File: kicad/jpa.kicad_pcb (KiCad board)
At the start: 2 copper layers, 3 parts, among them J1 ARM_NOAH_6PIN, J2 ARM_10PIN, J3 ARM_NOAH_5PIN

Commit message: layout, gerbers, models done
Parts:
- added J4: PICKIT_HDR, kicadlib:TH_6X1_HDR, F.Cu at (140.0, 98.7)
- moved J3 0.95 mm to (156.3, 108.0)
- moved J1 0.66 mm to (156.3, 97.7)
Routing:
- net /icspclk/swdclk: track 0.00 -> 36.8 mm, vias 0 -> 2
- net /icspdat/swdio: track 0.00 -> 31.2 mm, vias 0 -> 1
- net /swo/lvp: track 0.00 -> 29.2 mm, vias 0 -> 2
- net /mclr/nreset: track 0.00 -> 20.0 mm, vias 0 -> 1
- net /vcc: track 0.00 -> 19.4 mm
- added copper zone on B.Cu, net GND
- added copper zone on F.Cu, net GND
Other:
- board outline added: 24.9 x 20.8 mm
- board text added: "1"
- board text added: "JST PROG ADAPT V1"
- board text added: "github.com/noahp/jpa v1"
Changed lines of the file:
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@@
-(kicad_pcb (version 4) (host pcbnew 4.0.0-rc2-stable)
+(kicad_pcb (version 4) (host pcbnew 4.0.0-rc1-stable)
   (general
-    (links 13)
-    (no_connects 13)
-    (area 0 0 0 0)
+    (links 19)
+    (no_connects 6)
+    (area 136.322999 94.158999 161.522 115.137001)
     (thickness 1.6)
-    (drawings 0)
-    (tracks 0)
+    (drawings 11)
+    (tracks 52)
     (zones 0)
-    (modules 3)
+    (modules 4)
     (nets 9)
   )
@@
   (setup
     (last_trace_width 0.25)
+    (user_trace_width 0.35)
     (trace_clearance 0.2)
     (zone_clearance 0.508)
@@
     (pad_to_mask_clearance 0.2)
     (aux_axis_origin 0 0)
-    (visible_elements FFFFFF7F)
+    (visible_elements 7FFFFFFF)
     (pcbplotparams
-      (layerselection 0x00030_80000001)
+      (layerselection 0x010f0_80000001)
       (usegerberextensions false)
       (excludeedgelayer true)
@@
       (outputformat 1)
       (mirror false)
-      (drillshape 1)
+      (drillshape 0)
       (scaleselection 1)
-      (outputdirectory ""))
+      (outputdirectory gerbers))
   )
   (net 0 "")
@@
   )
   (module kicadlib:SMD_JST_6_PIN_VERT (layer F.Cu)
-    (at 156.3 97 270)
-    (fp_text reference J1 (at 2.6 1.8 270) (layer F.SilkS)
+    (at 156.337 97.663 270)
+    (fp_text reference J1 (at 0.028 1.868 360) (layer F.SilkS)
       (effects (font (size 0.75 0.75) (thickness 0.12)))
     )
@@
   )
   (module kicadlib:ARM_10_PIN (layer F.Cu)
-    (at 148.5011 105.0036)
+    (at 148.463 105.029)
     (fp_text reference J2 (at -0.635 -7.4) (layer F.SilkS)
       (effects (font (size 0.75 0.75) (thickness 0.12)))
@@
   )
   (module kicadlib:SMD_JST_5_PIN_VERT (layer F.Cu)
-    (at 156.3 107 270)
-    (fp_text reference J3 (at 2.6 1.8 270) (layer F.SilkS)
+    (at 156.337 107.95 270)
+    (fp_text reference J3 (at -0.066 1.995 360) (layer F.SilkS)
       (effects (font (size 0.75 0.75) (thickness 0.12)))
     )
@@
     )
   )
+  (module kicadlib:TH_6X1_HDR (layer F.Cu)
+    (at 139.954 98.679 270)
+    (fp_text reference J4 (at -1.905 0.127 360) (layer F.SilkS)
+      (effects (font (size 0.75 0.75) (thickness 0.12)))
+    )
+    (fp_text value PICKIT_HDR (at 14.986 0 360) (layer F.Fab)
+      (effects (font (size 0.75 0.75) (thickness 0.12)))
+    )
+    (pad 1 thru_hole rect (at 0 0 270) (size 2 2) (drill 1.2) (layers *.Cu *.Mask F.SilkS)
+      (net 4 /mclr/nreset))
+    (pad 2 thru_hole circle (at 2.54 0 270) (size 2 2) (drill 1.2) (layers *.Cu *.Mask F.SilkS)
+      (net 1 /vcc))
+    (pad 3 thru_hole circle (at 5.08 0 270) (size 2 2) (drill 1.2) (layers *.Cu *.Mask F.SilkS)
+      (net 6 GND))
+    (pad 4 thru_hole circle (at 7.62 0 270) (size 2 2) (drill 1.2) (layers *.Cu *.Mask F.SilkS)
+      (net 2 /icspdat/swdio))
+    (pad 5 thru_hole circle (at 10.16 0 270) (size 2 2) (drill 1.2) (layers *.Cu *.Mask F.SilkS)
+      (net 3 /icspclk/swdclk))
+    (pad 6 thru_hole circle (at 12.7 0 270) (size 2 2) (drill 1.2) (layers *.Cu *.Mask F.SilkS)
+      (net 5 /swo/lvp))
+    (model ${KIPRJMOD}/kicadlib/kicadlib.pretty/models/TH_6_PIN_HDR.wrl
+      (at (xyz -0.1 0 0.1))
+      (scale (xyz 0.395 0.395 0.395))
+      (rotate (xyz -90 0 0))
+    )
+  )
+  (gr_text "JST PROG ADAPT V1" (at 148.082 113.538) (layer F.Mask)
+    (effects (font (size 1 1) (thickness 0.15)))
+  )
+  (gr_text 1 (at 142.24 98.552) (layer F.SilkS)
+    (effects (font (size 1.5 1.5) (thickness 0.3)))
+  )
+  (gr_text "github.com/noahp/jpa\nv1" (at 157.734 104.648 270) (layer B.Mask)
+    (effects (font (size 1 1) (thickness 0.15)) (justify mirror))
+  )
+  (gr_line (start 136.398 113.03) (end 136.398 96.266) (angle 90) (layer Edge.Cuts) (width 0.15))
+  (gr_line (start 159.258 115.062) (end 138.43 115.062) (angle 90) (layer Edge.Cuts) (width 0.15))
+  (gr_line (start 161.29 96.266) (end 161.29 113.03) (angle 90) (layer Edge.Cuts) (width 0.15))
+  (gr_arc (start 138.43 113.03) (end 138.43 115.062) (angle 90) (layer Edge.Cuts) (width 0.15))
+  (gr_arc (start 159.258 113.03) (end 161.29 113.03) (angle 90) (layer Edge.Cuts) (width 0.15))
+  (gr_line (start 159.258 94.234) (end 138.43 94.234) (angle 90) (layer Edge.Cuts) (width 0.15))
+  (gr_arc (start 159.258 96.266) (end 159.258 94.234) (angle 90) (layer Edge.Cuts) (width 0.15))
+  (gr_arc (start 138.43 96.266) (end 136.398 96.266) (angle 90) (layer Edge.Cuts) (width 0.15))
+  (segment (start 147.828 102.489) (end 147.828 101.639) (width 0.35) (layer F.Cu) (net 1))
+  (segment (start 147.828 101.639) (end 151.804 97.663) (width 0.35) (layer F.Cu) (net 1))
+  (segment (start 151.804 97.663) (end 155.1495 97.663) (width 0.35) (layer F.Cu) (net 1))
+  (segment (start 155.1495 97.663) (end 156.337 97.663) (width 0.35) (layer F.Cu) (net 1))
+  (segment (start 139.954 101.219) (end 141.224 102.489) (width 0.35) (layer F.Cu) (net 1))
+  (segment (start 141.224 102.489) (end 147.828 102.489) (width 0.35) (layer F.Cu) (net 1))
+  (segment (start 149.098 102.489) (end 149.098 101.781894) (width 0.35) (layer B.Cu) (net 2))
+  (segment (start 149.098 101.781894) (end 148.930105 101.613999) (width 0.35) (layer B.Cu) (net 2))
+  (segment (start 148.930105 101.613999) (end 144.639001 101.613999) (width 0.35) (layer B.Cu) (net 2))
+  (segment (start 144.639001 101.613999) (end 140.953999 105.299001) (width 0.35) (layer B.Cu) (net 2))
+  (segment (start 140.953999 105.299001) (end 139.954 106.299) (width 0.35) (layer B.Cu) (net 2))
+  (segment (start 150.749 103.505) (end 150.749 104.5495) (width 0.35) (layer F.Cu) (net 2))
+  (segment (start 150.749 104.5495) (end 155.1495 108.95) (width 0.35) (layer F.Cu) (net 2))
+  (segment (start 155.1495 108.95) (end 156.337 108.95) (width 0.35) (layer F.Cu) (net 2))
+  (segment (start 149.098 102.489) (end 149.733 102.489) (width 0.35) (layer B.Cu) (net 2))
+  (segment (start 149.733 102.489) (end 150.749 103.505) (width 0.35) (layer B.Cu) (net 2))
+  (via (at 150.749 103.505) (size 0.6) (drill 0.4) (layers F.Cu B.Cu) (net 2))
+  (segment (start 149.098 102.489) (end 152.924 98.663) (width 0.35) (layer F.Cu) (net 2))
+  (segment (start 152.924 98.663) (end 156.337 98.663) (width 0.35) (layer F.Cu) (net 2))
+  (segment (start 151.511 111.125) (end 149.225 108.839) (width 0.35) (layer F.Cu) (net 3))
+  (segment (start 149.225 108.839) (end 139.954 108.839) (width 0.35) (layer F.Cu) (net 3))
+  (segment (start 152.654 109.855) (end 152.654 109.982) (width 0.35) (layer B.Cu) (net 3))
+  (segment (start 152.654 109.982) (end 151.511 111.125) (width 0.35) (layer B.Cu) (net 3))
+  (via (at 151.511 111.125) (size 0.6) (drill 0.4) (layers F.Cu B.Cu) (net 3))
+  (segment (start 156.337 109.95) (end 152.749 109.95) (width 0.35) (layer F.Cu) (net 3))
+  (segment (start 152.749 109.95) (end 152.654 109.855) (width 0.35) (layer F.Cu) (net 3))
+  (via (at 152.654 109.855) (size 0.6) (drill 0.4) (layers F.Cu B.Cu) (net 3))
+  (segment (start 149.098 103.759) (end 153.194 99.663) (width 0.35) (layer F.Cu) (net 3))
+  (segment (start 153.194 99.663) (end 156.337 99.663) (width 0.35) (layer F.Cu) (net 3))
+  (segment (start 156.305 99.695) (end 156.337 99.663) (width 0.35) (layer F.Cu) (net 3))
+  (segment (start 149.098 103.759) (end 155.289 109.95) (width 0.35) (layer F.Cu) (net 3))
+  (segment (start 155.289 109.95) (end 156.337 109.95) (width 0.35) (layer F.Cu) (net 3))
+  (segment (start 154.432 100.711) (end 156.289 100.711) (width 0.35) (layer F.Cu) (net 4))
+  (segment (start 156.289 100.711) (end 156.337 100.663) (width 0.35) (layer F.Cu) (net 4))
+  (segment (start 153.797 103.505) (end 153.797 101.346) (width 0.35) (layer B.Cu) (net 4))
+  (segment (start 153.797 101.346) (end 154.432 100.711) (width 0.35) (layer B.Cu) (net 4))
+  (via (at 154.432 100.711) (size 0.6) (drill 0.4) (layers F.Cu B.Cu) (net 4))
+  (segment (start 150.232999 107.069001) (end 153.797 103.505) (width 0.35) (layer B.Cu) (net 4))
+  (segment (start 149.098 107.569) (end 149.597999 107.069001) (width 0.35) (layer B.Cu) (net 4))
+  (segment (start 149.597999 107.069001) (end 150.232999 107.069001) (width 0.35) (layer B.Cu) (net 4))
+  (segment (start 149.098 107.569) (end 152.479 110.95) (width 0.35) (layer F.Cu) (net 4))
+  (segment (start 152.479 110.95) (end 156.337 110.95) (width 0.35) (layer F.Cu) (net 4))
+  (segment (start 153.797 105.918) (end 148.336 111.379) (width 0.35) (layer B.Cu) (net 5))
+  (segment (start 148.336 111.379) (end 139.954 111.379) (width 0.35) (layer B.Cu) (net 5))
+  (segment (start 154.369 101.663) (end 154.369 105.346) (width 0.35) (layer F.Cu) (net 5))
+  (segment (start 154.369 105.346) (end 153.797 105.918) (width 0.35) (layer F.Cu) (net 5))
+  (via (at 153.797 105.918) (size 0.6) (drill 0.4) (layers F.Cu B.Cu) (net 5))
+  (segment (start 151.765 104.267) (end 154.369 101.663) (width 0.35) (layer F.Cu) (net 5))
+  (segment (start 154.369 101.663) (end 156.337 101.663) (width 0.35) (layer F.Cu) (net 5))
+  (segment (start 149.098 105.029) (end 151.003 105.029) (width 0.35) (layer B.Cu) (net 5))
+  (segment (start 151.003 105.029) (end 151.765 104.267) (width 0.35) (layer B.Cu) (net 5))
+  (via (at 151.765 104.267) (size 0.6) (drill 0.4) (layers F.Cu B.Cu) (net 5))
+  (zone (net 6) (net_name GND) (layer F.Cu) (hatch edge 0.508)
+    (connect_pads (clearance 0.508))
+    (min_thickness 0.254)
+    (fill yes (arc_segments 16) (thermal_gap 0.508) (thermal_bridge_width 0.508))
+    (polygon
+      (pts
+        (xy 161.29 115.062) (xy 136.398 115.062) (xy 136.398 94.234) (xy 161.29 94.234) (xy 161.29 115.062)
+      )
+    )
+  )
+  (zone (net 6) (net_name GND) (layer B.Cu) (hatch edge 0.508)
+    (connect_pads (clearance 0.508))
+    (min_thickness 0.254)
+    (fill yes (arc_segments 16) (thermal_gap 0.508) (thermal_bridge_width 0.508))
+    (polygon
+      (pts
+        (xy 161.29 115.062) (xy 136.398 115.062) (xy 136.398 94.234) (xy 161.29 94.234) (xy 161.29 115.062)
+      )
+    )
+  )

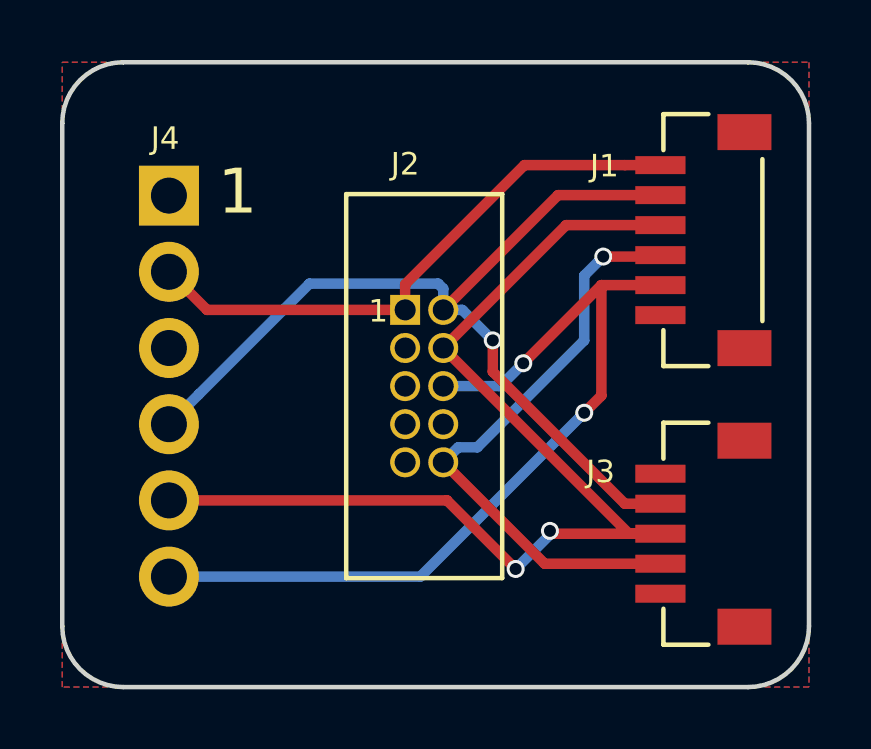
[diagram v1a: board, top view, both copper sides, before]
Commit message: fix some unconnected nets on the layout
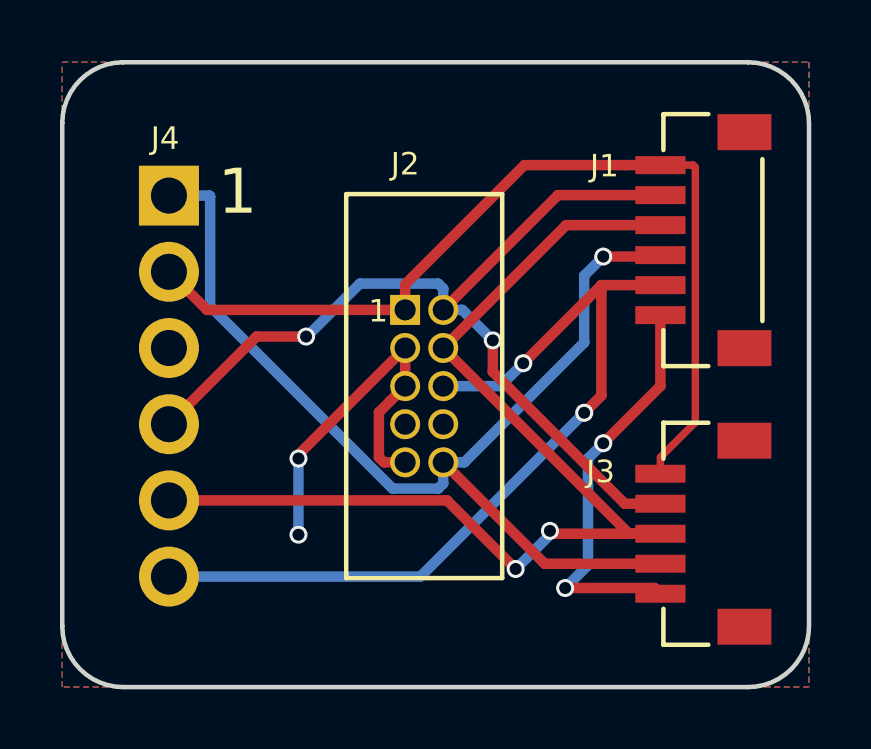
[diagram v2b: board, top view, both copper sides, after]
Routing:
- net GND: track 0.00 -> 26.3 mm, vias 0 -> 4
- net /mclr/nreset: track 20.0 -> 36.2 mm
- net /vcc: track 19.4 -> 31.3 mm
- net /icspdat/swdio: vias 1 -> 2
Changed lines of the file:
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@@
   (general
     (links 19)
-    (no_connects 6)
-    (area 136.322999 94.158999 161.522 115.137001)
+    (no_connects 0)
+    (area 136.322999 94.158999 161.365001 115.137001)
     (thickness 1.6)
     (drawings 11)
-    (tracks 52)
+    (tracks 86)
     (zones 0)
     (modules 4)
@@
   )
   (setup
-    (last_trace_width 0.25)
+    (last_trace_width 0.35)
     (user_trace_width 0.35)
     (trace_clearance 0.2)
@@
   (gr_arc (start 159.258 96.266) (end 159.258 94.234) (angle 90) (layer Edge.Cuts) (width 0.15))
   (gr_arc (start 138.43 96.266) (end 136.398 96.266) (angle 90) (layer Edge.Cuts) (width 0.15))
+  (segment (start 156.337 107.95) (end 156.337 107.4) (width 0.25) (layer F.Cu) (net 1))
+  (segment (start 156.337 107.4) (end 157.499501 106.237499) (width 0.25) (layer F.Cu) (net 1))
+  (segment (start 157.499501 106.237499) (end 157.499501 97.738001) (width 0.25) (layer F.Cu) (net 1))
+  (segment (start 157.499501 97.738001) (end 157.4245 97.663) (width 0.25) (layer F.Cu) (net 1))
+  (segment (start 157.4245 97.663) (end 156.337 97.663) (width 0.25) (layer F.Cu) (net 1))
   (segment (start 147.828 102.489) (end 147.828 101.639) (width 0.35) (layer F.Cu) (net 1))
   (segment (start 147.828 101.639) (end 151.804 97.663) (width 0.35) (layer F.Cu) (net 1))
@@
   (segment (start 139.954 101.219) (end 141.224 102.489) (width 0.35) (layer F.Cu) (net 1))
   (segment (start 141.224 102.489) (end 147.828 102.489) (width 0.35) (layer F.Cu) (net 1))
+  (segment (start 144.526 103.378) (end 142.875 103.378) (width 0.35) (layer F.Cu) (net 2))
+  (segment (start 142.875 103.378) (end 139.954 106.299) (width 0.35) (layer F.Cu) (net 2))
+  (segment (start 146.317795 101.613999) (end 144.553794 103.378) (width 0.35) (layer B.Cu) (net 2))
+  (segment (start 148.930105 101.613999) (end 146.317795 101.613999) (width 0.35) (layer B.Cu) (net 2))
+  (segment (start 144.553794 103.378) (end 144.526 103.378) (width 0.35) (layer B.Cu) (net 2))
+  (via (at 144.526 103.378) (size 0.6) (drill 0.4) (layers F.Cu B.Cu) (net 2))
   (segment (start 149.098 102.489) (end 149.098 101.781894) (width 0.35) (layer B.Cu) (net 2))
   (segment (start 149.098 101.781894) (end 148.930105 101.613999) (width 0.35) (layer B.Cu) (net 2))
-  (segment (start 148.930105 101.613999) (end 144.639001 101.613999) (width 0.35) (layer B.Cu) (net 2))
-  (segment (start 144.639001 101.613999) (end 140.953999 105.299001) (width 0.35) (layer B.Cu) (net 2))
-  (segment (start 140.953999 105.299001) (end 139.954 106.299) (width 0.35) (layer B.Cu) (net 2))
   (segment (start 150.749 103.505) (end 150.749 104.5495) (width 0.35) (layer F.Cu) (net 2))
   (segment (start 150.749 104.5495) (end 155.1495 108.95) (width 0.35) (layer F.Cu) (net 2))
@@
   (segment (start 149.098 103.759) (end 155.289 109.95) (width 0.35) (layer F.Cu) (net 3))
   (segment (start 155.289 109.95) (end 156.337 109.95) (width 0.35) (layer F.Cu) (net 3))
+  (segment (start 149.098 107.569) (end 149.098 108.276106) (width 0.35) (layer B.Cu) (net 4))
+  (segment (start 149.098 108.276106) (end 148.930105 108.444001) (width 0.35) (layer B.Cu) (net 4))
+  (segment (start 148.930105 108.444001) (end 147.407999 108.444001) (width 0.35) (layer B.Cu) (net 4))
+  (segment (start 147.407999 108.444001) (end 141.329001 102.365003) (width 0.35) (layer B.Cu) (net 4))
+  (segment (start 141.304 98.679) (end 139.954 98.679) (width 0.35) (layer B.Cu) (net 4))
+  (segment (start 141.329001 102.365003) (end 141.329001 98.704001) (width 0.35) (layer B.Cu) (net 4))
+  (segment (start 141.329001 98.704001) (end 141.304 98.679) (width 0.35) (layer B.Cu) (net 4))
+  (segment (start 149.098 107.569) (end 149.805106 107.569) (width 0.35) (layer B.Cu) (net 4))
+  (segment (start 149.805106 107.569) (end 153.797 103.577106) (width 0.35) (layer B.Cu) (net 4))
+  (segment (start 153.797 103.577106) (end 153.797 101.346) (width 0.35) (layer B.Cu) (net 4))
+  (segment (start 153.797 101.346) (end 154.432 100.711) (width 0.35) (layer B.Cu) (net 4))
   (segment (start 154.432 100.711) (end 156.289 100.711) (width 0.35) (layer F.Cu) (net 4))
   (segment (start 156.289 100.711) (end 156.337 100.663) (width 0.35) (layer F.Cu) (net 4))
-  (segment (start 153.797 103.505) (end 153.797 101.346) (width 0.35) (layer B.Cu) (net 4))
-  (segment (start 153.797 101.346) (end 154.432 100.711) (width 0.35) (layer B.Cu) (net 4))
   (via (at 154.432 100.711) (size 0.6) (drill 0.4) (layers F.Cu B.Cu) (net 4))
-  (segment (start 150.232999 107.069001) (end 153.797 103.505) (width 0.35) (layer B.Cu) (net 4))
-  (segment (start 149.098 107.569) (end 149.597999 107.069001) (width 0.35) (layer B.Cu) (net 4))
-  (segment (start 149.597999 107.069001) (end 150.232999 107.069001) (width 0.35) (layer B.Cu) (net 4))
   (segment (start 149.098 107.569) (end 152.479 110.95) (width 0.35) (layer F.Cu) (net 4))
   (segment (start 152.479 110.95) (end 156.337 110.95) (width 0.35) (layer F.Cu) (net 4))
@@
   (segment (start 151.003 105.029) (end 151.765 104.267) (width 0.35) (layer B.Cu) (net 5))
   (via (at 151.765 104.267) (size 0.6) (drill 0.4) (layers F.Cu B.Cu) (net 5))
+  (segment (start 147.828 105.029) (end 147.828 103.759) (width 0.35) (layer F.Cu) (net 6))
+  (segment (start 153.162 111.76) (end 156.147 111.76) (width 0.35) (layer F.Cu) (net 6))
+  (segment (start 156.147 111.76) (end 156.337 111.95) (width 0.35) (layer F.Cu) (net 6))
+  (segment (start 153.924 107.442) (end 153.924 110.998) (width 0.35) (layer B.Cu) (net 6))
+  (segment (start 153.924 110.998) (end 153.162 111.76) (width 0.35) (layer B.Cu) (net 6))
+  (via (at 153.162 111.76) (size 0.6) (drill 0.4) (layers F.Cu B.Cu) (net 6))
+  (segment (start 154.432 106.934) (end 153.924 107.442) (width 0.35) (layer B.Cu) (net 6))
+  (segment (start 156.337 102.663) (end 156.337 105.029) (width 0.35) (layer F.Cu) (net 6))
+  (via (at 154.432 106.934) (size 0.6) (drill 0.4) (layers F.Cu B.Cu) (net 6))
+  (segment (start 156.337 105.029) (end 154.432 106.934) (width 0.35) (layer F.Cu) (net 6))
+  (segment (start 144.272 107.442) (end 144.272 109.982) (width 0.35) (layer B.Cu) (net 6))
+  (via (at 144.272 107.442) (size 0.6) (drill 0.4) (layers F.Cu B.Cu) (net 6))
+  (segment (start 144.272 107.315) (end 144.272 107.442) (width 0.35) (layer F.Cu) (net 6))
+  (segment (start 147.828 103.759) (end 144.272 107.315) (width 0.35) (layer F.Cu) (net 6))
+  (via (at 144.272 109.982) (size 0.6) (drill 0.4) (layers F.Cu B.Cu) (net 6))
+  (segment (start 147.828 107.569) (end 147.120894 107.569) (width 0.35) (layer F.Cu) (net 6))
+  (segment (start 147.120894 107.569) (end 146.952999 107.401105) (width 0.35) (layer F.Cu) (net 6))
+  (segment (start 146.952999 107.401105) (end 146.952999 105.904001) (width 0.35) (layer F.Cu) (net 6))
+  (segment (start 146.952999 105.904001) (end 147.328001 105.528999) (width 0.35) (layer F.Cu) (net 6))
+  (segment (start 147.328001 105.528999) (end 147.828 105.029) (width 0.35) (layer F.Cu) (net 6))
   (zone (net 6) (net_name GND) (layer F.Cu) (hatch edge 0.508)
     (connect_pads (clearance 0.508))

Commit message: new renders, tighter layout (only saves ~0.60$ osh cost)
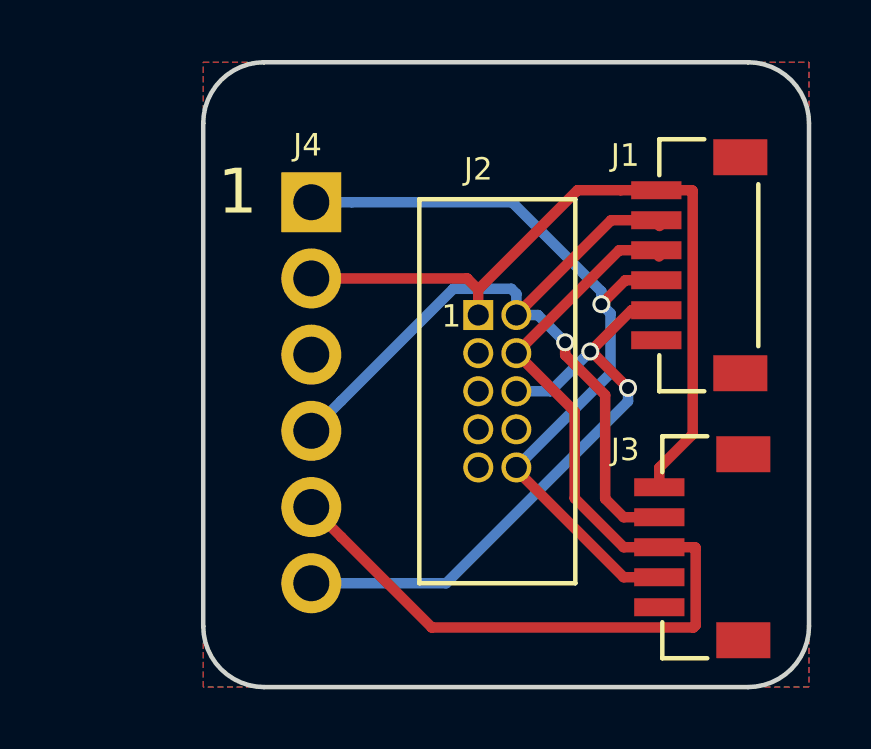
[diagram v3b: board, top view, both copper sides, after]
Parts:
- moved J4 4.75 mm to (144.7, 98.9)
- moved J2 2.44 mm to (150.9, 105.2)
- moved J1 0.85 mm to (156.2, 98.5)
- moved J3 0.45 mm to (156.3, 108.4)
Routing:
- net GND: track 26.3 -> 0.00 mm, vias 4 -> 0
- net /mclr/nreset: track 36.2 -> 26.7 mm
- net /swo/lvp: track 29.2 -> 21.1 mm
- net /vcc: track 31.3 -> 25.4 mm
- net /icspdat/swdio: track 31.2 -> 25.4 mm, vias 2 -> 1
- net /icspclk/swdclk: track 36.8 -> 33.6 mm, vias 2 -> 0
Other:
- board size 24.9 x 20.8 mm -> 20.2 x 20.8 mm
